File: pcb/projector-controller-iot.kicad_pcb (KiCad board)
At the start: 2 copper layers, 60 x 60 mm, 31 parts, among them J1 DE9_Pins, J2 USB_C_Receptacle, J3 Conn_01x04_Socket, J4 Conn_01x04_Socket, J5 Barrel_Jack, U1 ESP32-S3-WROOM-1, U2 SP3232EEN-L/TR, U3 LP5907MFX-3.3

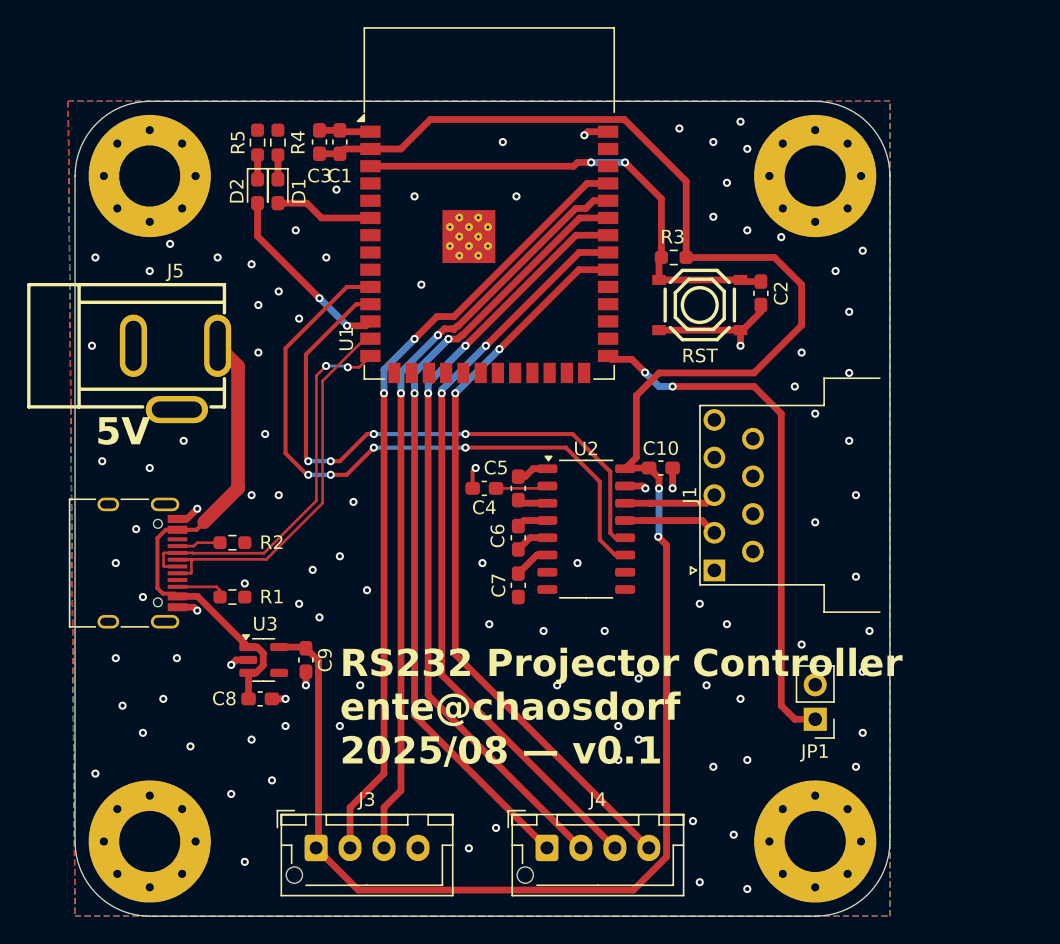
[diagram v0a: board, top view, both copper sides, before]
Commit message: make the esp not stick out
Signed-off-by: 3nt3 <gott@3nt3.de>
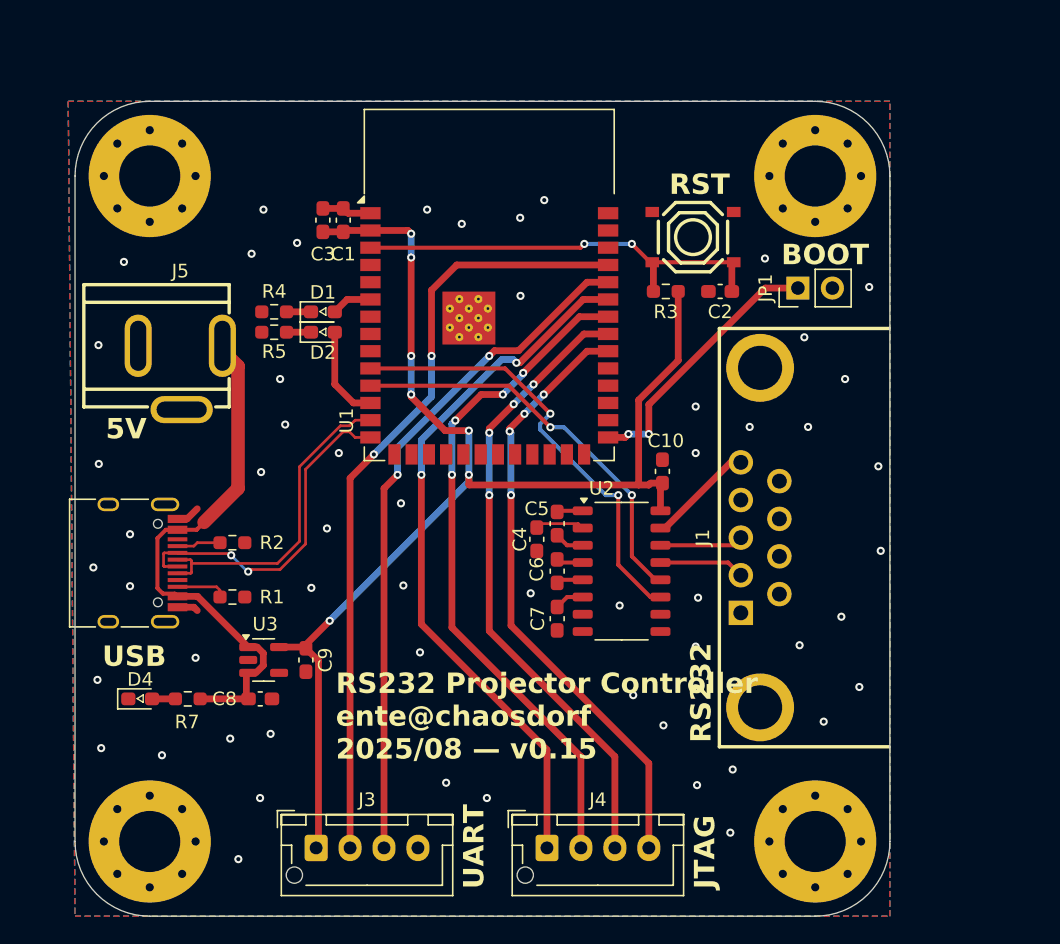
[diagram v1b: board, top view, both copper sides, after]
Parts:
- added D4: LED, kicad-lib:LED_0603_1608Metric_Pad1.05x0.95mm_HandSolder_Triangle, F.Cu at (144.3, 103.5)
- added R7: 1K5, Resistor_SMD:R_0603_1608Metric_Pad0.98x0.95mm_HandSolder, F.Cu at (147.8, 103.5)
- D1, D2: footprint LED_SMD:LED_0603_1608Metric_Pad1.05x0.95mm_HandSolder -> kicad-lib:LED_0603_1608Metric_Pad1.05x0.95mm_HandSolder_Triangle
- J1: footprint Connector_Dsub:DSUB-9_Pins_Horizontal_P2.77x2.84mm_EdgePinOffset9.40mm -> easyeda2kicad:DB9-TH_LD09P33E4GV00LF
- moved JP1 31.8 mm to (192.7, 73.2), turned to 90 degrees
- moved R5 14.0 mm to (154.2, 76.5), turned to 180 degrees
- moved R4 12.5 mm to (154.2, 75.0), turned to 180 degrees
- moved D2 11.4 mm to (157.8, 76.5), turned to 0 degrees
- moved D1 9.47 mm to (157.8, 75.0), turned to 0 degrees
- moved U1 6.00 mm to (170.0, 73.0)
- moved C1 5.76 mm to (159.2, 68.2)
- moved C3 5.76 mm to (157.8, 68.2)
- moved C4 5.38 mm to (173.5, 91.8), turned to -90 degrees
- moved SW1 5.02 mm to (185.0, 69.5), turned to 0 degrees
- moved J1 4.14 mm to (189.9, 91.6)
- moved U2 4.05 mm to (179.7, 94.1)
- moved C5 3.86 mm to (175.0, 90.6)
- moved C6 3.77 mm to (175.0, 94.1)
- moved C7 3.77 mm to (175.0, 97.6)
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- renumbered RST to SW1
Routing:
- net +3V3: track 144.2 -> 94.7 mm, vias 2 -> 7
- net Net-(JP1-A): track 38.9 -> 19.8 mm
- net U1TX: track 48.1 -> 33.1 mm, vias 4 -> 2
- net U1RX: track 44.2 -> 29.9 mm, vias 4 -> 2
- net GND: track 26.8 -> 14.9 mm, vias 103 -> 56
- net TCK: track 54.4 -> 44.7 mm, vias 2 -> 4
- net TDO: track 55.4 -> 46.3 mm, vias 2 -> 4
- net TDI: track 56.6 -> 50.0 mm, vias 2 -> 4
- net Net-(D2-A): track 13.6 -> 7.03 mm, vias 2 -> 0
- net TMS: track 58.0 -> 52.1 mm
- net U0RX: track 56.1 -> 50.4 mm
- net USB_D+: track 29.2 -> 23.8 mm
- net Net-(U1-EN): track 36.2 -> 31.8 mm
- net Net-(D1-A): track 7.26 -> 3.00 mm
- net USB_D-: track 28.7 -> 25.4 mm
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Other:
- board text added: "BOOT"
- board text added: "JTAG"
- board text added: "RS232"
- board text added: "RS232 Projector Controller ente@chaosdorf 2025/08 — v0.15"
- board text added: "RST"
- board text added: "UART"
- board text added: "USB"
- board text added: "i hate everything about this pcb"
- board text removed: "RS232 Projector Controller ente@chaosdorf 2025/08 — v0.1"
